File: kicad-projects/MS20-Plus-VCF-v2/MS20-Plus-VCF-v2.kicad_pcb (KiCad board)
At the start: 0 parts

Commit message: Added PCB for MS20 filter, and BOM for VCO
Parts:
- added C1: 1n, Capacitor_THT:C_Rect_L7.0mm_W3.5mm_P5.00mm, F.Cu at (256.1, 101.7)
- added C10: 100n, Capacitor_THT:C_Rect_L7.0mm_W3.5mm_P5.00mm, F.Cu at (228.5, 71.0)
- added C2: 1n, Capacitor_THT:C_Rect_L7.0mm_W3.5mm_P5.00mm, F.Cu at (232.7, 138.6)
- added C3: 10u, Capacitor_THT:CP_Radial_D5.0mm_P2.50mm, F.Cu at (231.4, 156.5)
- added C4: 47u, Capacitor_THT:CP_Radial_D6.3mm_P2.50mm, F.Cu at (262.6, 100.6)
- added C5: 47u, Capacitor_THT:CP_Radial_D6.3mm_P2.50mm, F.Cu at (214.7, 51.5)
- added C6: 100n, Capacitor_THT:C_Rect_L7.0mm_W3.5mm_P5.00mm, F.Cu at (208.2, 52.5)
- added C7: 100n, Capacitor_THT:C_Rect_L7.0mm_W3.5mm_P5.00mm, F.Cu at (227.6, 138.6)
- added C8: 47n, Capacitor_THT:C_Rect_L7.0mm_W3.5mm_P5.00mm, F.Cu at (270.9, 113.0)
- added C9: 100n, Capacitor_THT:C_Rect_L7.0mm_W3.5mm_P5.00mm, F.Cu at (249.7, 90.9)
- added D1: GREEN, LED_THT:LED_D3.0mm, F.Cu at (65.5, 67.2)
- added D2: GREEN, LED_THT:LED_D3.0mm, F.Cu at (70.0, 64.7)
- added D3: GREEN, LED_THT:LED_D3.0mm, F.Cu at (49.0, 109.3)
- added D4: GREEN, LED_THT:LED_D3.0mm, F.Cu at (44.5, 111.9)
- added D5: GREEN, LED_THT:LED_D3.0mm, F.Cu at (49.0, 88.2)
- added D6: GREEN, LED_THT:LED_D3.0mm, F.Cu at (44.5, 90.8)
- added J1: CV1, Connector_Audio:Jack_3.5mm_QingPu_WQP-PJ398SM_Vertical_CircularHoles, F.Cu at (57.5, 135.9)
- added J10: PanelC2, Connector_PinHeader_2.54mm:PinHeader_1x08_P2.54mm_Vertical, F.Cu at (40.2, 121.5)
- added J11: BackC2, Connector_PinSocket_2.54mm:PinSocket_1x08_P2.54mm_Vertical, F.Cu at (123.8, 121.5)
- added J2: CV2, Connector_Audio:Jack_3.5mm_QingPu_WQP-PJ398SM_Vertical_CircularHoles, F.Cu at (57.5, 150.5)
- added J3: CV3, Connector_Audio:Jack_3.5mm_QingPu_WQP-PJ398SM_Vertical_CircularHoles, F.Cu at (67.9, 135.9)
- added J4: Out, Connector_Audio:Jack_3.5mm_QingPu_WQP-PJ398SM_Vertical_CircularHoles, F.Cu at (67.9, 150.5)
- added J5: HP_In, Connector_Audio:Jack_3.5mm_QingPu_WQP-PJ398SM_Vertical_CircularHoles, F.Cu at (47.1, 135.9)
- added J6: LP_In, Connector_Audio:Jack_3.5mm_QingPu_WQP-PJ398SM_Vertical_CircularHoles, F.Cu at (47.1, 150.5)
- added J7: EURPower, Connector_IDC:IDC-Header_2x05_P2.54mm_Vertical, F.Cu at (211.8, 158.0)
- added J8: PanelC1, Connector_PinHeader_2.54mm:PinHeader_1x08_P2.54mm_Vertical, F.Cu at (74.7, 121.5)
- added J9: BackC1, Connector_PinSocket_2.54mm:PinSocket_1x08_P2.54mm_Vertical, F.Cu at (89.3, 121.5)
- added Q1: Q, Package_TO_SOT_THT:TO-92_Inline, F.Cu at (243.8, 156.6)
- added Q2: Q, Package_TO_SOT_THT:TO-92_Inline, F.Cu at (237.9, 156.6)
- added R1: 220R, Resistor_THT:R_Axial_DIN0207_L6.3mm_D2.5mm_P7.62mm_Horizontal, F.Cu at (243.5, 109.2)
- added R10: 100k, Resistor_THT:R_Axial_DIN0207_L6.3mm_D2.5mm_P7.62mm_Horizontal, F.Cu at (256.6, 112.6)
- added R11: 10k, Resistor_THT:R_Axial_DIN0207_L6.3mm_D2.5mm_P7.62mm_Horizontal, F.Cu at (226.3, 82.0)
- added R12: 10k, Resistor_THT:R_Axial_DIN0207_L6.3mm_D2.5mm_P7.62mm_Horizontal, F.Cu at (247.6, 109.2)
- added R13: 220R, Resistor_THT:R_Axial_DIN0207_L6.3mm_D2.5mm_P7.62mm_Horizontal, F.Cu at (218.2, 85.4)
- added R14: 13k, Resistor_THT:R_Axial_DIN0207_L6.3mm_D2.5mm_P7.62mm_Horizontal, F.Cu at (227.2, 92.7)
- added R15: 220R, Resistor_THT:R_Axial_DIN0207_L6.3mm_D2.5mm_P7.62mm_Horizontal, F.Cu at (270.4, 124.0)
- added R16: 10k, Resistor_THT:R_Axial_DIN0207_L6.3mm_D2.5mm_P7.62mm_Horizontal, F.Cu at (266.4, 134.7)
- added R17: 1k, Resistor_THT:R_Axial_DIN0207_L6.3mm_D2.5mm_P7.62mm_Horizontal, F.Cu at (266.4, 113.2)
- added R18: 1k, Resistor_THT:R_Axial_DIN0207_L6.3mm_D2.5mm_P7.62mm_Horizontal, F.Cu at (214.2, 85.4)
- added R19: 10k, Resistor_THT:R_Axial_DIN0207_L6.3mm_D2.5mm_P7.62mm_Horizontal, F.Cu at (207.7, 63.5)
- added R2: 13k, Resistor_THT:R_Axial_DIN0207_L6.3mm_D2.5mm_P7.62mm_Horizontal, F.Cu at (245.2, 98.5)
- added R20: NC, Resistor_THT:R_Axial_DIN0207_L6.3mm_D2.5mm_P7.62mm_Horizontal, F.Cu at (231.3, 92.7)
- added R21: NC, Resistor_THT:R_Axial_DIN0207_L6.3mm_D2.5mm_P7.62mm_Horizontal, F.Cu at (251.6, 101.8)
- added R22: 4k7, Resistor_THT:R_Axial_DIN0207_L6.3mm_D2.5mm_P7.62mm_Horizontal, F.Cu at (223.2, 92.7)
- added R23: 0R, Resistor_THT:R_Axial_DIN0207_L6.3mm_D2.5mm_P7.62mm_Horizontal, F.Cu at (207.7, 74.3)
- added R24: 4k7, Resistor_THT:R_Axial_DIN0207_L6.3mm_D2.5mm_P7.62mm_Horizontal, F.Cu at (252.5, 112.6)
- added R25: 68k, Resistor_THT:R_Axial_DIN0207_L6.3mm_D2.5mm_P7.62mm_Horizontal, F.Cu at (230.4, 82.0)
- added R26: 4k7, Resistor_THT:R_Axial_DIN0207_L6.3mm_D2.5mm_P7.62mm_Horizontal, F.Cu at (237.1, 96.4)
- added R27: 0R, Resistor_THT:R_Axial_DIN0207_L6.3mm_D2.5mm_P7.62mm_Horizontal, F.Cu at (223.9, 71.2)
- added R28: 470R, Resistor_THT:R_Axial_DIN0207_L6.3mm_D2.5mm_P7.62mm_Horizontal, F.Cu at (211.8, 74.3)
- added R29: 10R, Resistor_THT:R_Axial_DIN0207_L6.3mm_D2.5mm_P7.62mm_Horizontal, F.Cu at (272.4, 157.0)
- added R3: 220R, Resistor_THT:R_Axial_DIN0207_L6.3mm_D2.5mm_P7.62mm_Horizontal, F.Cu at (270.4, 134.7)
- added R30: 10R, Resistor_THT:R_Axial_DIN0207_L6.3mm_D2.5mm_P7.62mm_Horizontal, F.Cu at (211.8, 63.5)
- added R31: 4k7, Resistor_THT:R_Axial_DIN0207_L6.3mm_D2.5mm_P7.62mm_Horizontal, F.Cu at (235.3, 85.6)
- added R32: 470k, Resistor_THT:R_Axial_DIN0207_L6.3mm_D2.5mm_P7.62mm_Horizontal, F.Cu at (215.8, 63.9)
- added R4: 1k, Resistor_THT:R_Axial_DIN0207_L6.3mm_D2.5mm_P7.62mm_Horizontal, F.Cu at (241.1, 96.4)
- added R5: 10k, Resistor_THT:R_Axial_DIN0207_L6.3mm_D2.5mm_P7.62mm_Horizontal, F.Cu at (260.6, 112.6)
- added R6: 10k, Resistor_THT:R_Axial_DIN0207_L6.3mm_D2.5mm_P7.62mm_Horizontal, F.Cu at (215.8, 74.7)
- added R7: 100k, Resistor_THT:R_Axial_DIN0207_L6.3mm_D2.5mm_P7.62mm_Horizontal, F.Cu at (266.4, 124.0)
- added R8: 100k, Resistor_THT:R_Axial_DIN0207_L6.3mm_D2.5mm_P7.62mm_Horizontal, F.Cu at (222.3, 82.0)
- added R9: 100k, Resistor_THT:R_Axial_DIN0207_L6.3mm_D2.5mm_P7.62mm_Horizontal, F.Cu at (219.9, 71.2)
- added REF**: MountingHole_3mm_Pad, MountingHole:MountingHole_3mm_Pad, F.Cu at (57.4, 55.2)
- added REF**: MountingHole_3mm_Pad, MountingHole:MountingHole_3mm_Pad, F.Cu at (122.2, 114.2)
- added REF**: MountingHole_3mm_Pad, MountingHole:MountingHole_3mm_Pad, F.Cu at (106.3, 55.2)
- added REF**: MountingHole_3mm_Pad, MountingHole:MountingHole_3mm_Pad, F.Cu at (73.2, 114.2)
- added RV1: 100k, Potentiometer_THT:Potentiometer_Alpha_RD901F-40-00D_Single_Vertical, F.Cu at (65.2, 85.9)
- added RV10: 2k, Potentiometer_THT:Potentiometer_Bourns_3296W_Vertical, F.Cu at (173.4, 104.5)
- added RV2: 100k, Potentiometer_THT:Potentiometer_Alpha_RD901F-40-00D_Single_Vertical, F.Cu at (65.1, 107.0)
- added RV3: 100k, Potentiometer_THT:Potentiometer_Alpha_RD901F-40-00D_Single_Vertical, F.Cu at (65.3, 62.4)
- added RV4: 100k, Potentiometer_THT:Potentiometer_Alpha_RD901F-40-00D_Single_Vertical, F.Cu at (44.4, 62.3)
- added RV5: 100k, Potentiometer_THT:Potentiometer_Alpha_RD901F-40-00D_Single_Vertical, F.Cu at (44.2, 85.9)
- added RV6: 100k, Potentiometer_THT:Potentiometer_Alpha_RD901F-40-00D_Single_Vertical, F.Cu at (44.2, 107.0)
- added RV7: 50k, Potentiometer_THT:Potentiometer_Bourns_3296W_Vertical, F.Cu at (267.6, 139.3)
- added RV8: 50k, Potentiometer_THT:Potentiometer_Bourns_3296W_Vertical, F.Cu at (267.1, 150.5)
- added RV9: 50k, Potentiometer_THT:Potentiometer_Bourns_3296W_Vertical, F.Cu at (208.9, 78.9)
- added SW1: BP_Select, Switches:5mm_rocker_toggle_switch, F.Cu at (57.1, 115.0)
- added U1: LM13700, Package_DIP:DIP-16_W7.62mm, F.Cu at (230.2, 149.6)
- added U2: TL074, Package_DIP:DIP-14_W7.62mm, F.Cu at (207.8, 140.4)
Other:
- board outline added: 87 x 100 mm
- copper layers 0 -> 2

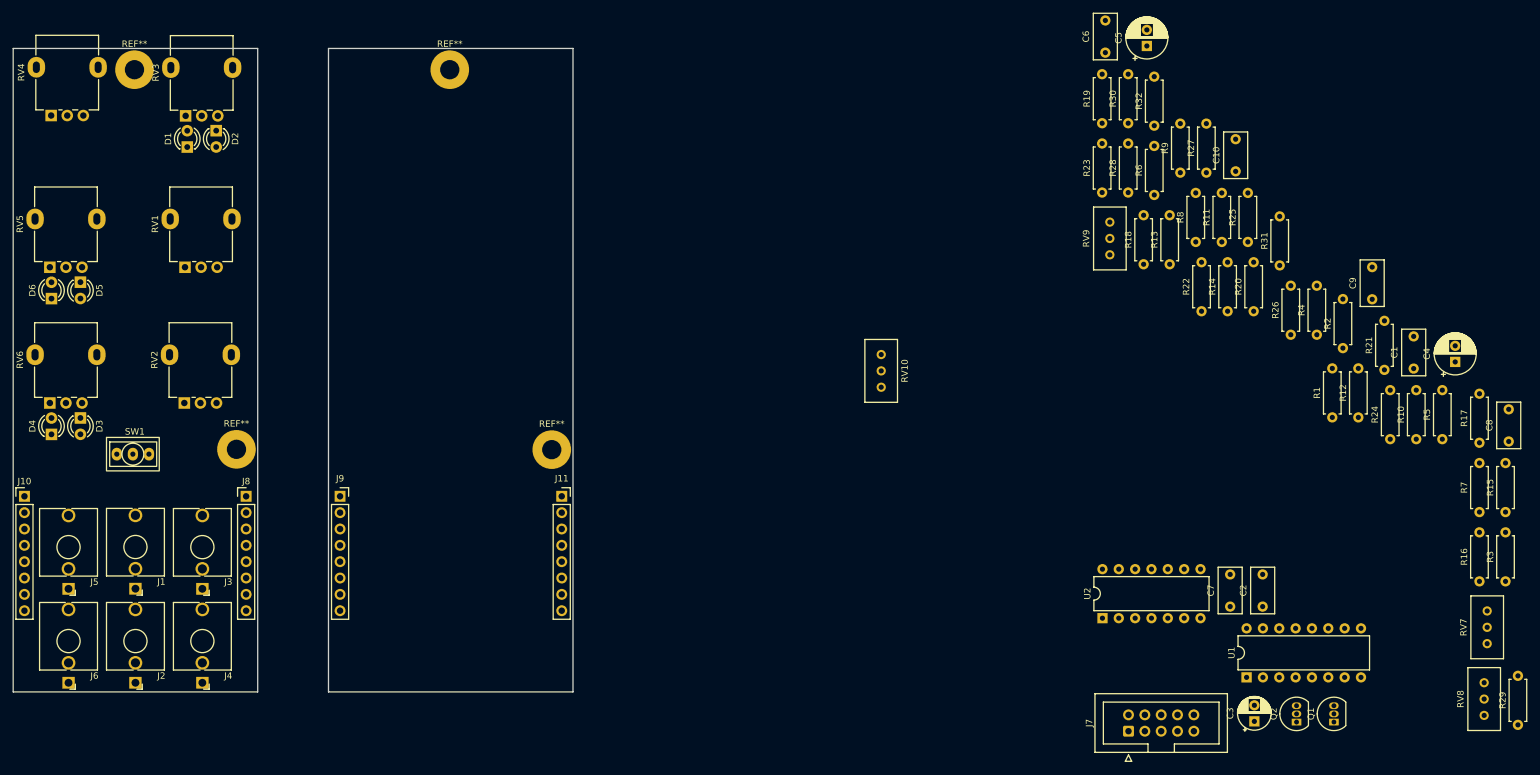
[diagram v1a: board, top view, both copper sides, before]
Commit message: More work on the MS20 VCF. Closing in on a final placement.
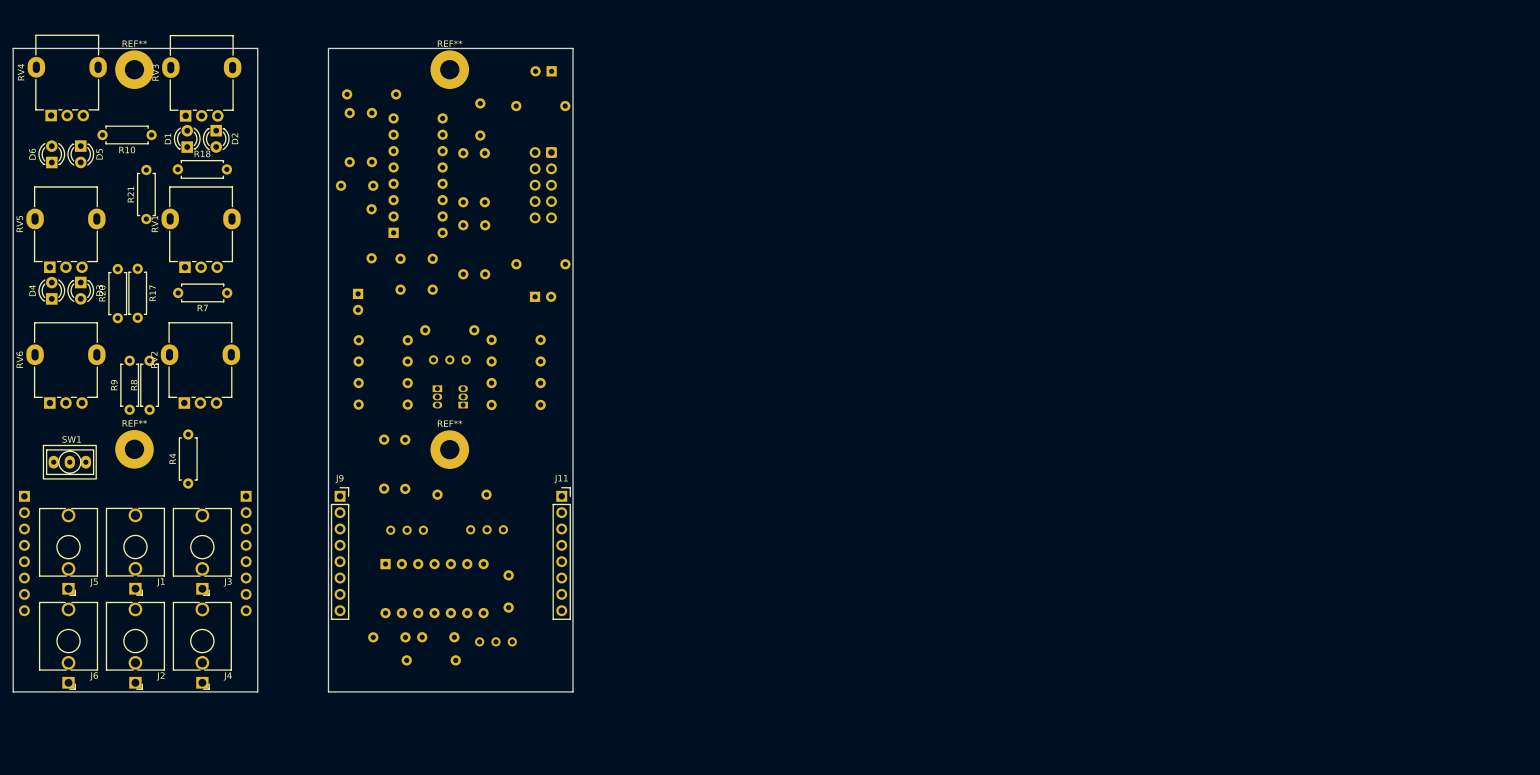
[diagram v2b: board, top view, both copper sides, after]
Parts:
- C1, C10, C2, C3, C4, C5, C6, C7, C8, C9, J10, J7, J8, Q1, Q2, R1, R11, R12, R13, R14, R15, R16, R19, R2, R22, R23, R24, R25, R26, R27, R28, R29, R3, R30, R31, R32, R5, R6, RV10, RV7, RV8, RV9, U1, U2: moved to B.Cu
- moved R17 210.3 mm to (57.9, 86.1), turned to -90 degrees
- moved R10 202.1 mm to (60.0, 65.3), turned to 180 degrees
- moved R7 197.6 mm to (71.8, 89.9), turned to 180 degrees
- moved R21 193.8 mm to (59.2, 78.4)
- moved R15 191.4 mm to (90.4, 59.0), turned to 0 degrees
- moved R16 190.1 mm to (90.8, 61.9), turned to -90 degrees
- moved C8 179.1 mm to (94.5, 143.4), turned to 0 degrees
- moved R4 176.9 mm to (65.7, 119.5)
- moved R20 176.5 mm to (54.8, 93.8)
- moved R3 172.4 mm to (108.5, 75.8)
- moved R29 171.3 mm to (116.7, 85.4), turned to 0 degrees
- moved R9 167.4 mm to (56.6, 108.0)
- moved RV7 165.8 mm to (102.2, 126.8), turned to 0 degrees
- moved R8 164.7 mm to (59.7, 108.0)
- moved RV8 156.2 mm to (111.0, 144.1), turned to 180 degrees
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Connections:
- U2 pad 1: Net-(C8-Pad1) -> /SC_Res2
- U2 pad 10: /HP_In -> /LP_In
- U2 pad 12: /FRes -> GND
- U2 pad 13: /SC_Res1 -> Net-(C8-Pad2)
- U2 pad 14: /SC_Res2 -> Net-(C8-Pad1)
- U2 pad 2: Net-(C8-Pad2) -> /SC_Res1
- U2 pad 3: GND -> /FRes
- U2 pad 5: /LP_In -> /HP_In
- U2 pad 6: /SC_LpG1 -> /SC_HpG1
- U2 pad 7: /SC_LpG2 -> /SC_HpG2
- U2 pad 8: /SC_HpG2 -> /SC_LpG2
- U2 pad 9: /SC_HpG1 -> /SC_LpG1

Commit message: Tidied up
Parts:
- moved R23 21.0 mm to (117.2, 120.4)
- moved R27 14.5 mm to (99.8, 113.5)
- moved R22 14.3 mm to (113.7, 120.4)
- moved RV10 13.4 mm to (98.4, 108.7)
- moved RV7 7.72 mm to (109.9, 125.8), turned to 180 degrees
- moved RV9 5.88 mm to (103.8, 125.8), turned to 0 degrees
- moved R32 3.25 mm to (92.2, 100.7)
- moved R31 3.15 mm to (99.8, 104.1)
- moved R28 2.73 mm to (102.5, 100.7), turned to 0 degrees
- moved REF** 1.80 mm to (57.4, 116.0)
- moved REF** 1.75 mm to (106.3, 116.0)
- moved C9 1.65 mm to (116.1, 132.2)
- moved R12 1.55 mm to (102.5, 97.2)
- moved RV8 0.91 mm to (111.9, 144.1)
- moved U2 0.86 mm to (96.5, 131.2)
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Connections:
- J10 pad 2: /SC_LpG2_P -> /SC_Res1_P
- J10 pad 3: /SC_LpG1_P -> /SC_Res2_P
- J10 pad 6: /SC_Res2_P -> /SC_LpG1_P
- J10 pad 7: /SC_Res1_P -> /SC_LpG2_P
- J11 pad 2: /SC_LpG2 -> /SC_Res1
- J11 pad 3: /SC_LpG1 -> /SC_Res2
- J11 pad 6: /SC_Res2 -> /SC_LpG1
- J11 pad 7: /SC_Res1 -> /SC_LpG2
- J8 pad 1: GNDA -> /FOut_P
- J8 pad 2: -12VA -> +12VA
- J8 pad 3: /LP_In_P -> /CVMix_P
- J8 pad 6: /FOut_P -> GNDA
- J8 pad 7: /CVMix_P -> /LP_In_P
- J8 pad 8: +12VA -> -12VA
- J9 pad 1: GND -> /FOut
- J9 pad 2: -12V -> +12V
- J9 pad 3: /LP_In -> /CVMix
- J9 pad 6: /FOut -> GND
- J9 pad 7: /CVMix -> /LP_In
- J9 pad 8: +12V -> -12V
- U2 pad 1: /SC_Res2 -> /SC_HpG2
- U2 pad 2: /SC_Res1 -> /SC_HpG1
- U2 pad 3: /FRes -> /HP_In
- U2 pad 5: /HP_In -> /FRes
- U2 pad 6: /SC_HpG1 -> /SC_Res1
- U2 pad 7: /SC_HpG2 -> /SC_Res2

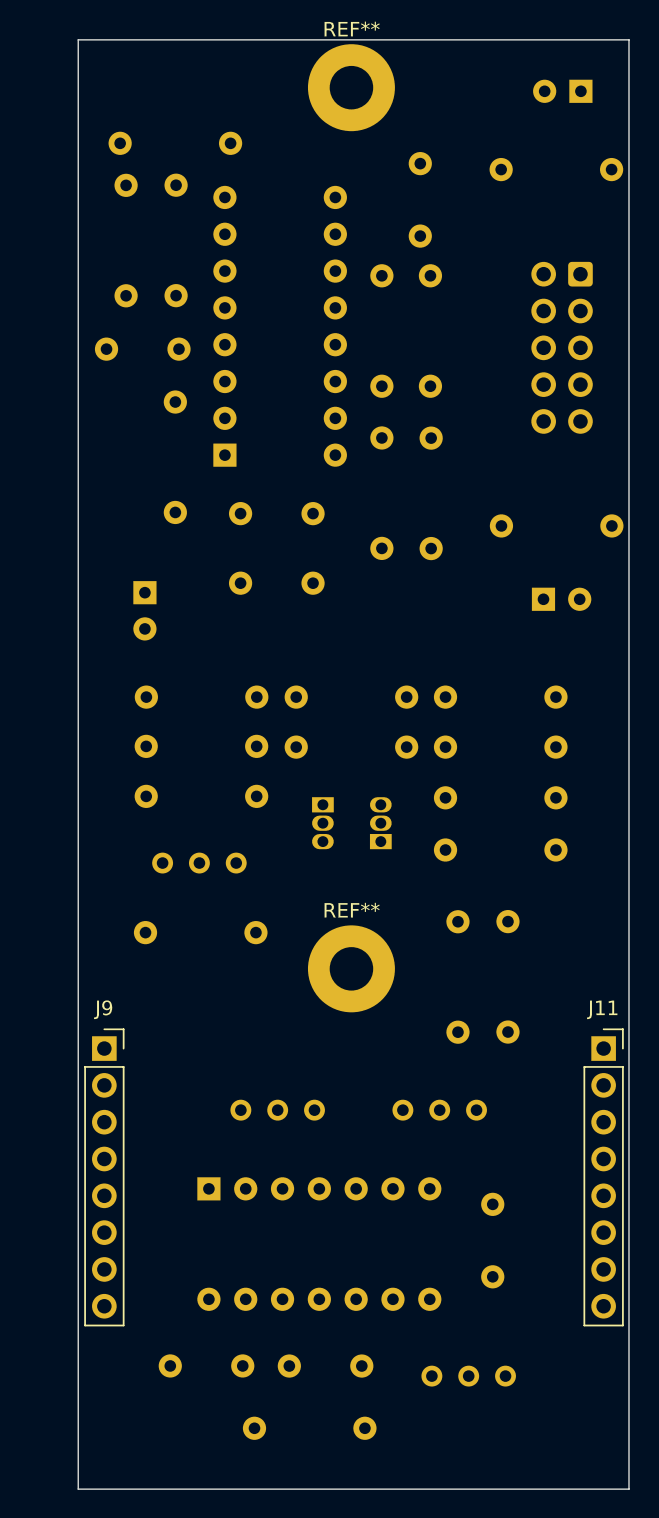
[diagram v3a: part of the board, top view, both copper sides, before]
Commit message: Almost done with main routing
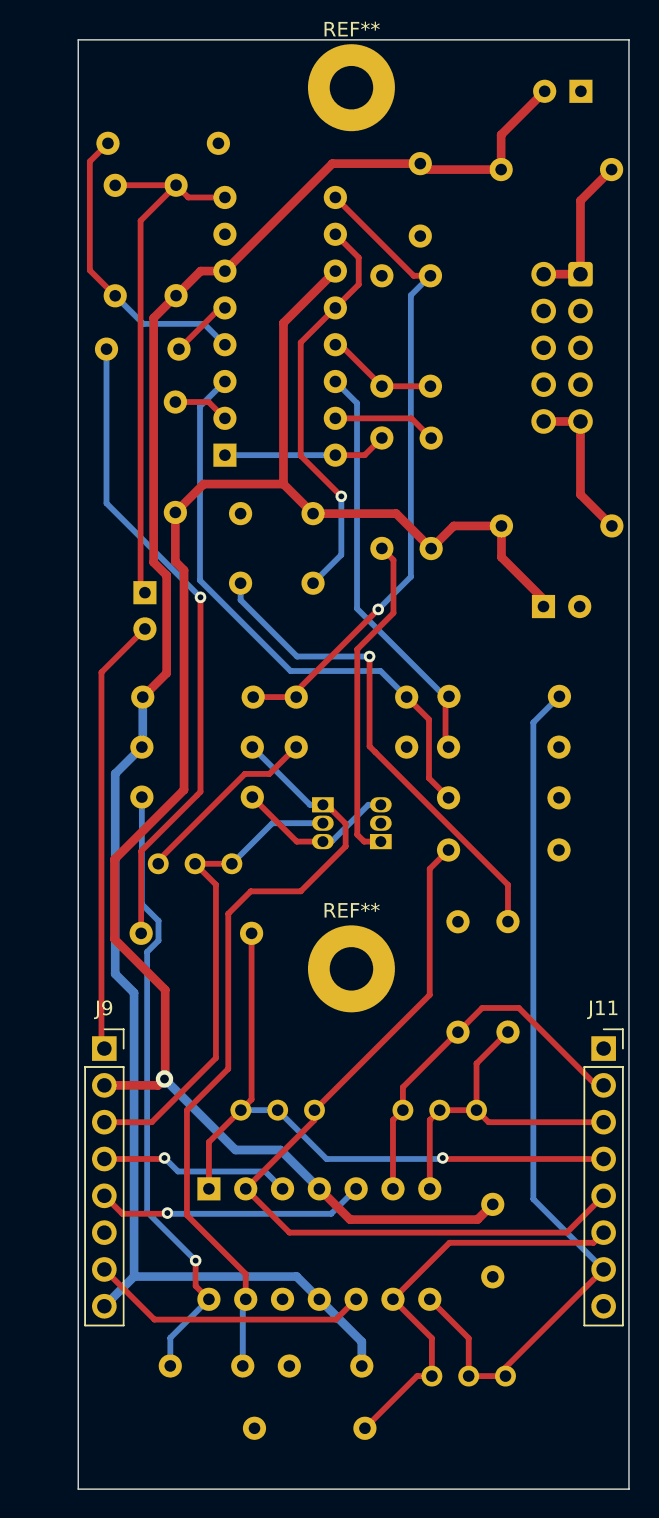
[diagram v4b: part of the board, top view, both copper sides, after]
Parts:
- moved R15 0.84 mm to (89.5, 59.0)
- moved R16 0.75 mm to (90.0, 61.9)
- moved C4 0.50 mm to (119.6, 91.0)
- moved R27 0.30 mm to (99.5, 113.5)
- moved RV10 0.30 mm to (98.1, 108.8)
- moved R31 0.30 mm to (99.5, 104.2)
- moved R32 0.30 mm to (91.9, 100.7)
- moved R11 0.25 mm to (92.0, 97.2)
- moved R25 0.25 mm to (120.7, 97.2)
- moved R1 0.21 mm to (113.0, 100.7)
- moved R13 0.21 mm to (113.0, 104.2)
- moved R26 0.21 mm to (113.0, 107.8)
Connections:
- REF** pad 1: (no net) -> GND (x2)
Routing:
- net -12V: track 0.00 -> 125.9 mm
- net +12V: track 0.00 -> 123.0 mm, vias 0 -> 1
- net /SC_LpG2: track 0.00 -> 61.4 mm
- net /SC_HpG1: track 0.00 -> 56.2 mm
- net Net-(C8-Pad2): track 0.00 -> 54.4 mm
- net /SC_HpG2: track 0.00 -> 45.3 mm, vias 0 -> 1
- net /FPole2: track 0.00 -> 44.7 mm, vias 0 -> 1
- net Net-(R11-Pad2): track 0.00 -> 44.7 mm, vias 0 -> 1
- net Net-(C8-Pad1): track 0.00 -> 42.9 mm, vias 0 -> 1
- net Net-(R12-Pad2): track 0.00 -> 40.2 mm
- net Net-(C3-Pad1): track 0.00 -> 37.2 mm
- net /FPole1: track 0.00 -> 33.9 mm, vias 0 -> 1
- net /CVMix: track 0.00 -> 33.5 mm
- net /FOut: track 0.00 -> 30.3 mm
- net /SC_LpG1: track 0.00 -> 29.0 mm
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
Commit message: Finished the layout
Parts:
- moved R10 15.0 mm to (55.5, 79.6), turned to 90 degrees
- moved D5 5.48 mm to (44.5, 70.2), turned to 90 degrees
- moved R18 5.28 mm to (59.0, 69.5), turned to 90 degrees
- moved D6 4.91 mm to (49.0, 67.7), turned to -90 degrees
- moved SW1 1.87 mm to (46.6, 114.5), turned to 180 degrees
- moved R17 1.25 mm to (59.0, 86.7)
- moved R9 1.23 mm to (55.5, 108.6)
- moved R21 1.23 mm to (59.0, 79.6)
- moved R15 1.16 mm to (89.8, 57.9)
- moved R8 0.94 mm to (59.0, 108.6)
- moved R20 0.93 mm to (55.5, 94.4)
- moved C3 0.90 mm to (91.2, 90.0)
- moved D3 0.52 mm to (49.0, 88.8)
- moved D4 0.52 mm to (44.5, 91.3)
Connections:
- REF** pad 1: (no net) -> GNDA (x2)
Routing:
- net /FRes_P: track 0.00 -> 97.7 mm, vias 0 -> 1
- net /FOut_P: track 0.00 -> 88.5 mm, vias 0 -> 2
- net /SC_HpG2_P: track 0.00 -> 88.1 mm
- net /SC_HpG1_P: track 0.00 -> 87.0 mm
- net -12VA: track 0.00 -> 83.7 mm
- net /SC_LpG1_P: track 0.00 -> 77.8 mm
- net /SC_LpG2_P: track 0.00 -> 76.8 mm
- net /LP_In_P: track 0.00 -> 74.6 mm, vias 0 -> 2
- net /SC_Res2_P: track 0.00 -> 73.2 mm, vias 0 -> 1
- net /CVMix_P: track 0.00 -> 73.2 mm, vias 0 -> 1
- net +12VA: track 0.00 -> 71.2 mm
- net /SC_Res1_P: track 0.00 -> 66.6 mm, vias 0 -> 1
- net /HP_In_P: track 0.00 -> 60.6 mm, vias 0 -> 1
- net Net-(J1-PadT): track 0.00 -> 48.5 mm, vias 0 -> 2
- net Net-(R18-Pad1): track 0.00 -> 45.0 mm, vias 0 -> 1
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- added copper zone on B.Cu, net GND
- added copper zone on F.Cu, net GND
- added copper zone on B.Cu, net GNDA
- added copper zone on F.Cu, net GNDA
